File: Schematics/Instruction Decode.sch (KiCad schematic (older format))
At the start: 10 parts, among them U50 GLS29EE010, U51 GLS29EE010, U52 74F574, U53 74F574, U54 74F574

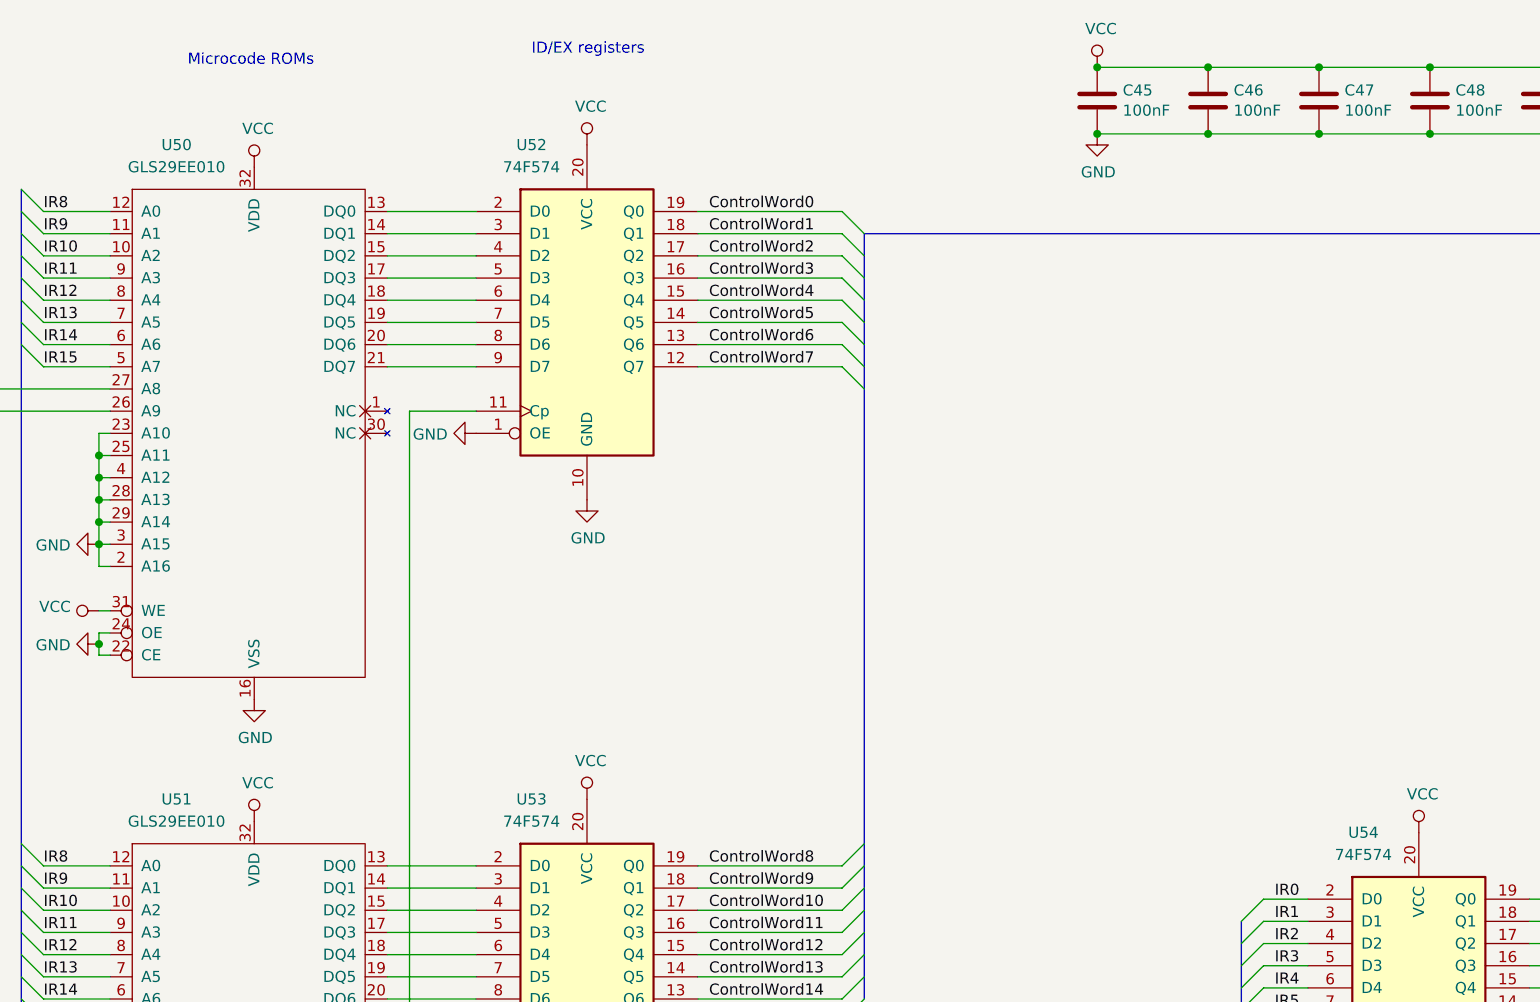
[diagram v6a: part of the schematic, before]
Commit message: Loosely group PCB footprints according to corresponding sheet.
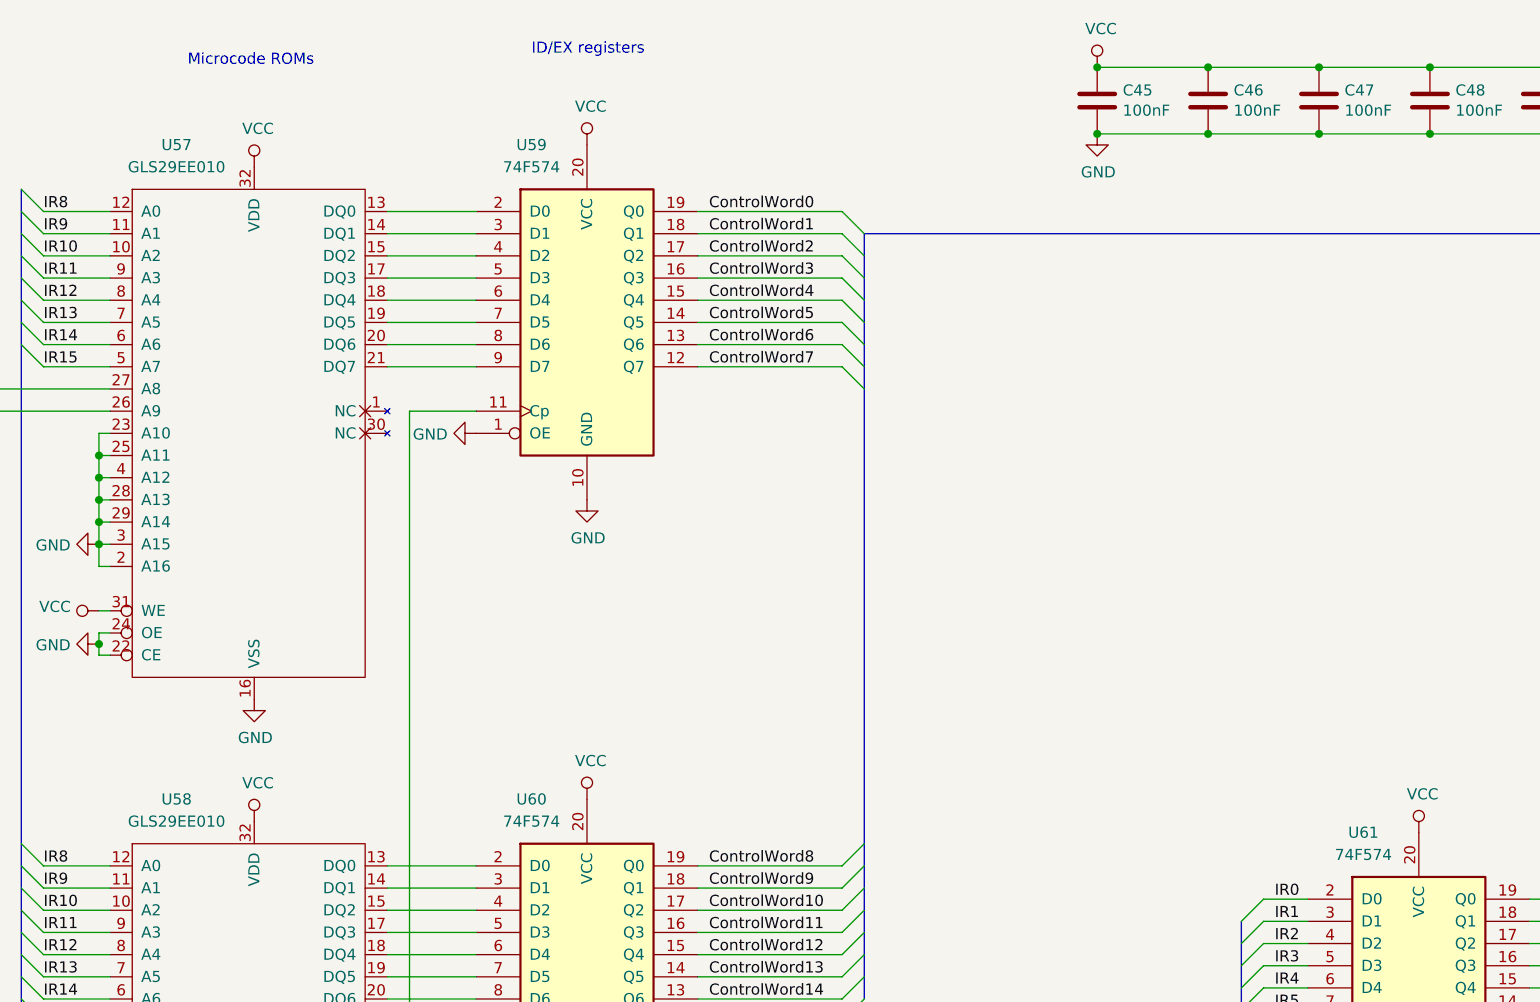
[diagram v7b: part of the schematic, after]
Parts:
- renumbered U50 to U57, U51 to U58, U52 to U59, U53 to U60, U54 to U61
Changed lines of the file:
@@
 P 2900 1250
 AR Path="/5D2C0AA0/5DB5EC09" Ref="U?"  Part="1"
-AR Path="/5D2C0B92/5DB5EC09" Ref="U50"  Part="1"
-F 0 "U50" H 2550 1450 50  0000 C CNN
+AR Path="/5D2C0B92/5DB5EC09" Ref="U57"  Part="1"
+F 0 "U57" H 2550 1450 50  0000 C CNN
 F 1 "GLS29EE010" H 2550 1350 50  0000 C CNN
 F 2 "Package_DIP:DIP-32_W15.24mm_Socket" H 2900 1250 50  0001 C CNN
@@
 P 2900 4200
 AR Path="/5D2C0AA0/5DB5EC5B" Ref="U?"  Part="1"
-AR Path="/5D2C0B92/5DB5EC5B" Ref="U51"  Part="1"
-F 0 "U51" H 2550 4400 50  0000 C CNN
+AR Path="/5D2C0B92/5DB5EC5B" Ref="U58"  Part="1"
+F 0 "U58" H 2550 4400 50  0000 C CNN
 F 1 "GLS29EE010" H 2550 4300 50  0000 C CNN
 F 2 "Package_DIP:DIP-32_W15.24mm_Socket" H 2900 4200 50  0001 C CNN
@@
 P 8150 4950
 AR Path="/5D2C14C3/5DB613F7" Ref="U?"  Part="1"
-AR Path="/5D2C0B92/5DB613F7" Ref="U54"  Part="1"
-F 0 "U54" H 7900 5750 50  0000 C CNN
+AR Path="/5D2C0B92/5DB613F7" Ref="U61"  Part="1"
+F 0 "U61" H 7900 5750 50  0000 C CNN
 F 1 "74F574" H 7900 5650 50  0000 C CNN
 F 2 "Package_DIP:DIP-20_W7.62mm" H 8150 4950 50  0001 C CNN
@@
 P 4400 1850
 AR Path="/5D2C14C3/5DB75B66" Ref="U?"  Part="1"
-AR Path="/5D2C0B92/5DB75B66" Ref="U52"  Part="1"
-F 0 "U52" H 4150 2650 50  0000 C CNN
+AR Path="/5D2C0B92/5DB75B66" Ref="U59"  Part="1"
+F 0 "U59" H 4150 2650 50  0000 C CNN
 F 1 "74F574" H 4150 2550 50  0000 C CNN
 F 2 "Package_DIP:DIP-20_W7.62mm" H 4400 1850 50  0001 C CNN
@@
 P 4400 4800
 AR Path="/5D2C14C3/5DB7864A" Ref="U?"  Part="1"
-AR Path="/5D2C0B92/5DB7864A" Ref="U53"  Part="1"
-F 0 "U53" H 4150 5600 50  0000 C CNN
+AR Path="/5D2C0B92/5DB7864A" Ref="U60"  Part="1"
+F 0 "U60" H 4150 5600 50  0000 C CNN
 F 1 "74F574" H 4150 5500 50  0000 C CNN
 F 2 "Package_DIP:DIP-20_W7.62mm" H 4400 4800 50  0001 C CNN
